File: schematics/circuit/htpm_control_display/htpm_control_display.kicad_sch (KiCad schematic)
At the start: 55 parts, among them J1 Conn_01x10_Socket, J2 Conn_01x10_Socket

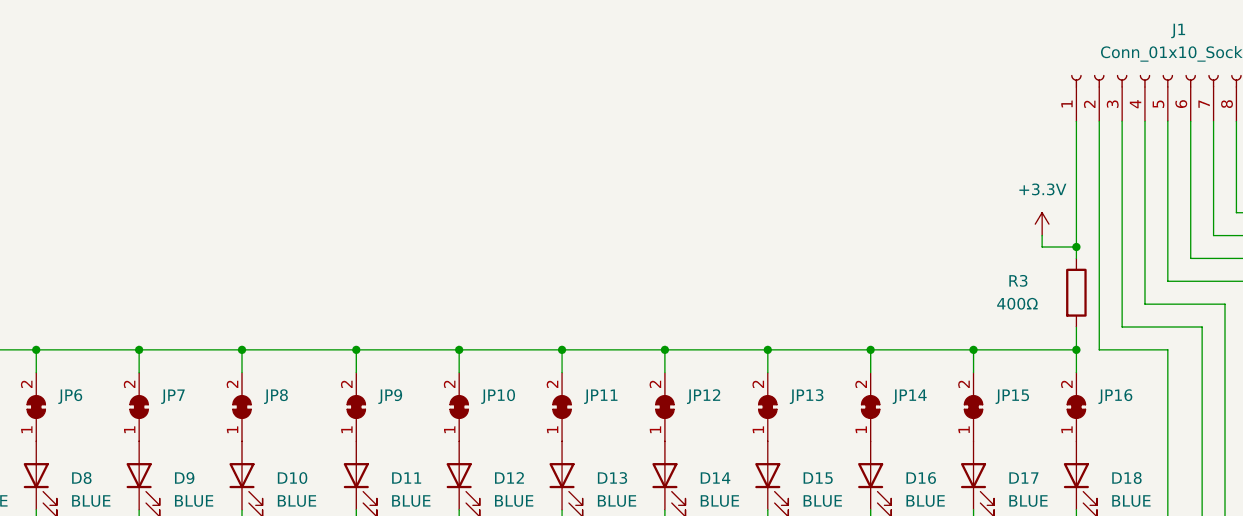
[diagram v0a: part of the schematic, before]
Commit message: Created HTPm CONTROL module display PCB.
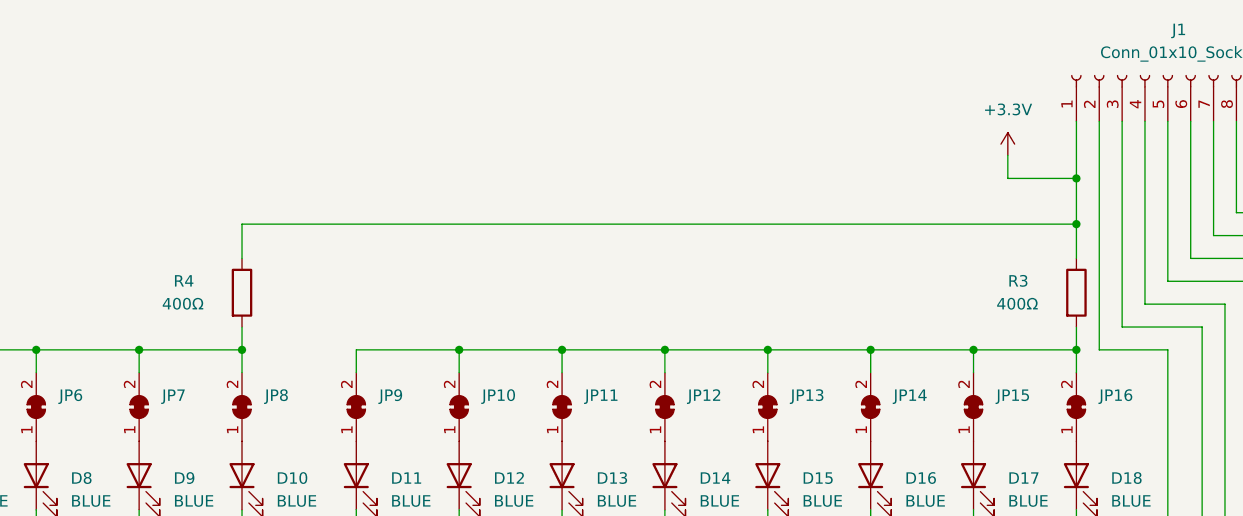
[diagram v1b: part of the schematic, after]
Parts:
- added R4: 400Ω, Resistor_THT:R_Axial_DIN0204_L3.6mm_D1.6mm_P7.62mm_Horizontal, symbol Device:R
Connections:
- net +3.3V: now also R4.1
- net at JP10.2 (B), JP11.2 (B), JP12.2 (B)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: no longer JP1.2 (B), JP2.2 (B), JP3.2 (B), JP4.2 (B), JP5.2 (B), JP6.2 (B), JP7.2 (B), JP8.2 (B)
- new net: JP1.2 (B), JP2.2 (B), JP3.2 (B), JP4.2 (B), JP5.2 (B), JP6.2 (B), JP7.2 (B), JP8.2 (B), R4.2
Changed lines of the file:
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@@
   (junction (at 242.57 88.9) (diameter 0) (color 0 0 0 0)
   )
+  (junction (at 135.89 57.15) (diameter 0) (color 0 0 0 0)
+  )
   (junction (at 171.45 57.15) (diameter 0) (color 0 0 0 0)
   )
@@
   (junction (at 101.6 57.15) (diameter 0) (color 0 0 0 0)
   )
-  (junction (at 135.89 57.15) (diameter 0) (color 0 0 0 0)
-  )
   (junction (at 135.89 77.47) (diameter 0) (color 0 0 0 0)
   )
+  (junction (at 228.6 38.1) (diameter 0) (color 0 0 0 0)
+  )
   (junction (at 217.17 57.15) (diameter 0) (color 0 0 0 0)
   )
@@
   (junction (at 257.81 104.14) (diameter 0) (color 0 0 0 0)
   )
+  (junction (at 228.6 43.18) (diameter 0) (color 0 0 0 0)
+  )
   (junction (at 90.17 77.47) (diameter 0) (color 0 0 0 0)
   )
   (junction (at 123.19 116.84) (diameter 0) (color 0 0 0 0)
   )
-  (junction (at 148.59 57.15) (diameter 0) (color 0 0 0 0)
-  )
-  (junction (at 228.6 45.72) (diameter 0) (color 0 0 0 0)
-  )
   (junction (at 115.57 96.52) (diameter 0) (color 0 0 0 0)
   )
@@
     (stroke (width 0) (type default))
   )
+  (wire (pts (xy 135.89 43.18) (xy 135.89 46.99))
+    (stroke (width 0) (type default))
+  )
   (wire (pts (xy 55.88 140.97) (xy 104.14 140.97))
     (stroke (width 0) (type default))
@@
     (stroke (width 0) (type default))
   )
+  (wire (pts (xy 220.98 35.56) (xy 220.98 38.1))
+    (stroke (width 0) (type default))
+  )
   (wire (pts (xy 148.59 74.93) (xy 148.59 77.47))
     (stroke (width 0) (type default))
@@
     (stroke (width 0) (type default))
   )
-  (wire (pts (xy 224.79 45.72) (xy 224.79 44.45))
-    (stroke (width 0) (type default))
-  )
-  (wire (pts (xy 228.6 45.72) (xy 224.79 45.72))
-    (stroke (width 0) (type default))
-  )
   (wire (pts (xy 217.17 57.15) (xy 228.6 57.15))
     (stroke (width 0) (type default))
@@
     (stroke (width 0) (type default))
   )
-  (wire (pts (xy 228.6 31.75) (xy 228.6 45.72))
+  (wire (pts (xy 228.6 31.75) (xy 228.6 38.1))
     (stroke (width 0) (type default))
   )
@@
     (stroke (width 0) (type default))
   )
+  (wire (pts (xy 228.6 38.1) (xy 228.6 43.18))
+    (stroke (width 0) (type default))
+  )
   (wire (pts (xy 252.73 99.06) (xy 252.73 113.03))
     (stroke (width 0) (type default))
@@
     (stroke (width 0) (type default))
   )
-  (wire (pts (xy 135.89 57.15) (xy 148.59 57.15))
-    (stroke (width 0) (type default))
-  )
   (wire (pts (xy 246.38 41.91) (xy 246.38 31.75))
     (stroke (width 0) (type default))
@@
     (stroke (width 0) (type default))
   )
-  (wire (pts (xy 228.6 45.72) (xy 228.6 46.99))
-    (stroke (width 0) (type default))
-  )
   (wire (pts (xy 236.22 31.75) (xy 236.22 52.07))
     (stroke (width 0) (type default))
@@
     (stroke (width 0) (type default))
   )
+  (wire (pts (xy 228.6 43.18) (xy 135.89 43.18))
+    (stroke (width 0) (type default))
+  )
   (wire (pts (xy 242.57 88.9) (xy 242.57 113.03))
     (stroke (width 0) (type default))
@@
     (stroke (width 0) (type default))
   )
+  (wire (pts (xy 220.98 38.1) (xy 228.6 38.1))
+    (stroke (width 0) (type default))
+  )
   (wire (pts (xy 160.02 57.15) (xy 148.59 57.15))
     (stroke (width 0) (type default))
@@
     (stroke (width 0) (type default))
   )
+  (wire (pts (xy 228.6 43.18) (xy 228.6 46.99))
+    (stroke (width 0) (type default))
+  )
   (wire (pts (xy 251.46 36.83) (xy 251.46 31.75))
     (stroke (width 0) (type default))
   )
   (wire (pts (xy 243.84 44.45) (xy 243.84 31.75))
+    (stroke (width 0) (type default))
+  )
+  (wire (pts (xy 135.89 54.61) (xy 135.89 57.15))
     (stroke (width 0) (type default))
   )
@@
     )
   )
+  (symbol (lib_id "Device:R") (at 135.89 50.8 0) (unit 1)
+    (in_bom yes) (on_board yes) (dnp no)
+    (property "Reference" "R4" (at 128.27 49.53 0)
+      (effects (font (size 1.27 1.27)) (justify left))
+    )
+    (property "Value" "400Ω" (at 127 52.07 0)
+      (effects (font (size 1.27 1.27)) (justify left))
+    )
+    (property "Footprint" "Resistor_THT:R_Axial_DIN0204_L3.6mm_D1.6mm_P7.62mm_Horizontal" (at 134.112 50.8 90)
+      (effects (font (size 1.27 1.27)) hide)
+    )
+    (property "Datasheet" "~" (at 135.89 50.8 0)
+      (effects (font (size 1.27 1.27)) hide)
+    )
+    (pin "1")
+    (pin "2")
+    (instances
+      (project "htpm_control_display"
+        (path "/5d804e4b-c61d-47d3-9254-644534119e0a"
+          (reference "R4") (unit 1)
+        )
+      )
+    )
+  )
   (symbol (lib_id "Device:LED") (at 205.74 71.12 90) (unit 1)
     (in_bom yes) (on_board yes) (dnp no) (fields_autoplaced)
@@
     )
   )
-  (symbol (lib_id "power:+3.3V") (at 224.79 44.45 0) (unit 1)
-    (in_bom yes) (on_board yes) (dnp no) (fields_autoplaced)
-    (property "Reference" "#PWR02" (at 224.79 48.26 0)
-      (effects (font (size 1.27 1.27)) hide)
-    )
-    (property "Value" "+3.3V" (at 224.79 39.37 0)
+  (symbol (lib_id "power:+3.3V") (at 220.98 35.56 0) (unit 1)
+    (in_bom yes) (on_board yes) (dnp no)
+    (property "Reference" "#PWR02" (at 220.98 39.37 0)
+      (effects (font (size 1.27 1.27)) hide)
+    )
+    (property "Value" "+3.3V" (at 220.98 30.48 0)
       (effects (font (size 1.27 1.27)))
     )
-    (property "Footprint" "" (at 224.79 44.45 0)
-      (effects (font (size 1.27 1.27)) hide)
-    )
-    (property "Datasheet" "" (at 224.79 44.45 0)
-      (effects (font (size 1.27 1.27)) hide)
-    )
+    (property "Footprint" "" (at 220.98 35.56 0)
+      (effects (font (size 1.27 1.27)) hide)
+    )
+    (property "Datasheet" "" (at 220.98 35.56 0)
+      (effects (font (size 1.27 1.27)) hide)
+    )

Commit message: Created HTPm CONTROL module display Gerbers.
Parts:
- added H1, H2: MountingHole, MountingHole:MountingHole_2.5mm, symbol Mechanical:MountingHole
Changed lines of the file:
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@@
+    )
+  )
+  (symbol (lib_id "Mechanical:MountingHole") (at 55.88 163.83 0) (unit 1)
+    (in_bom yes) (on_board yes) (dnp no) (fields_autoplaced)
+    (property "Reference" "H1" (at 58.42 162.56 0)
+      (effects (font (size 1.27 1.27)) (justify left))
+    )
+    (property "Value" "MountingHole" (at 58.42 165.1 0)
+      (effects (font (size 1.27 1.27)) (justify left))
+    )
+    (property "Footprint" "MountingHole:MountingHole_2.5mm" (at 55.88 163.83 0)
+      (effects (font (size 1.27 1.27)) hide)
+    )
+    (property "Datasheet" "~" (at 55.88 163.83 0)
+      (effects (font (size 1.27 1.27)) hide)
+    )
+    (instances
+      (project "htpm_control_display"
+        (path "/5d804e4b-c61d-47d3-9254-644534119e0a"
+          (reference "H1") (unit 1)
+        )
+      )
     )
   )
@@
         )
       )
+    )
+  )
+  (symbol (lib_id "Mechanical:MountingHole") (at 77.47 163.83 0) (unit 1)
+    (in_bom yes) (on_board yes) (dnp no) (fields_autoplaced)
+    (property "Reference" "H2" (at 80.01 162.56 0)
+      (effects (font (size 1.27 1.27)) (justify left))
+    )
+    (property "Value" "MountingHole" (at 80.01 165.1 0)
+      (effects (font (size 1.27 1.27)) (justify left))
+    )
+    (property "Footprint" "MountingHole:MountingHole_2.5mm" (at 77.47 163.83 0)
+      (effects (font (size 1.27 1.27)) hide)
+    )
+    (property "Datasheet" "~" (at 77.47 163.83 0)
+      (effects (font (size 1.27 1.27)) hide)
+    )
+    (instances
+      (project "htpm_control_display"
+        (path "/5d804e4b-c61d-47d3-9254-644534119e0a"
+          (reference "H2") (unit 1)
+        )
+      )
